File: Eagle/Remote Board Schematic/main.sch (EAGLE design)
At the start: 1 part

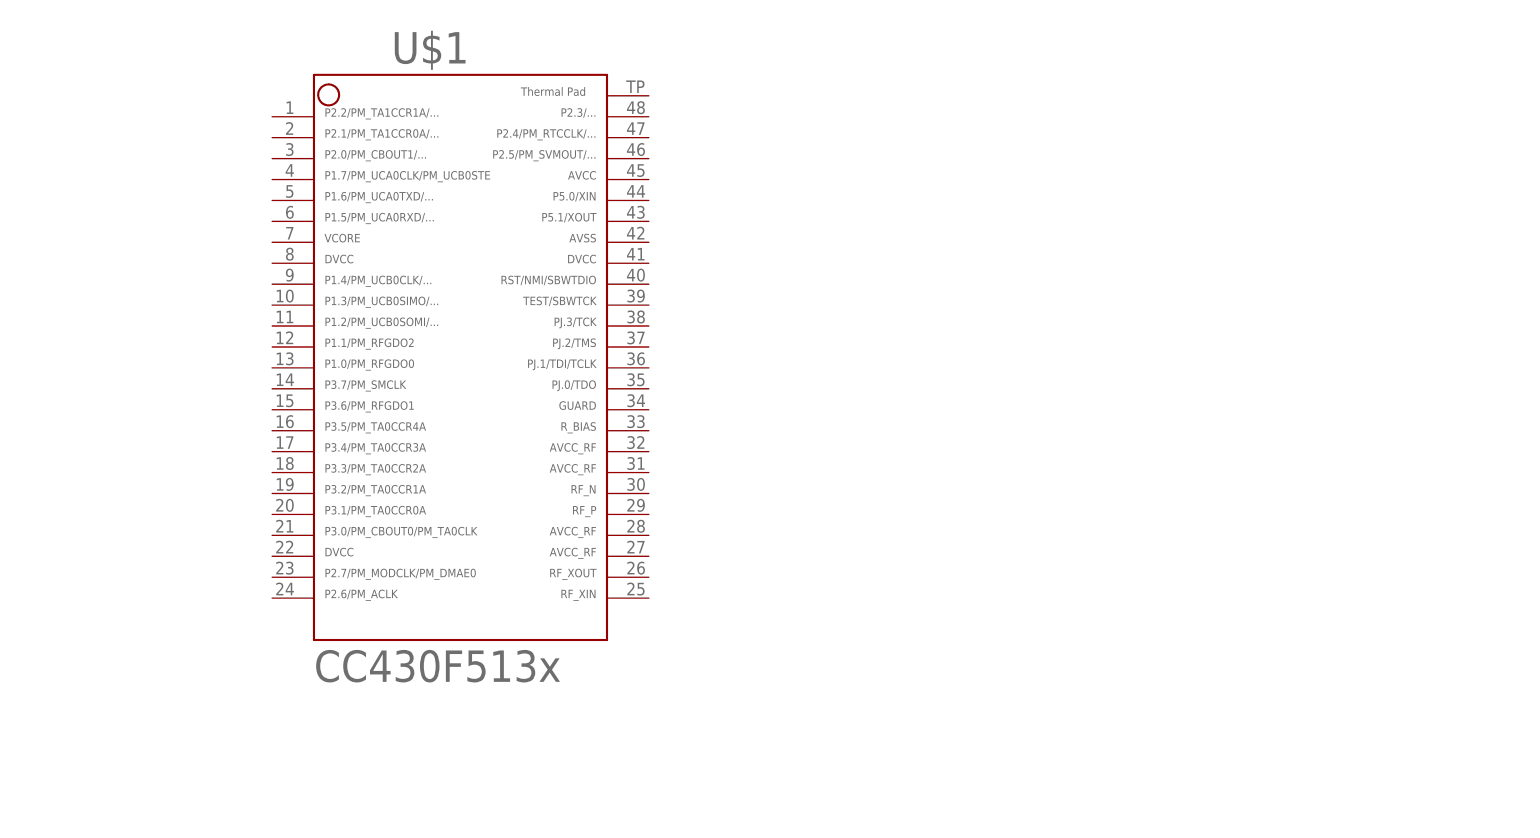
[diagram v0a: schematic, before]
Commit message: Schematic update
Set up skeleton for match network on RF path. Inductor footprint
probably needs to be changed.
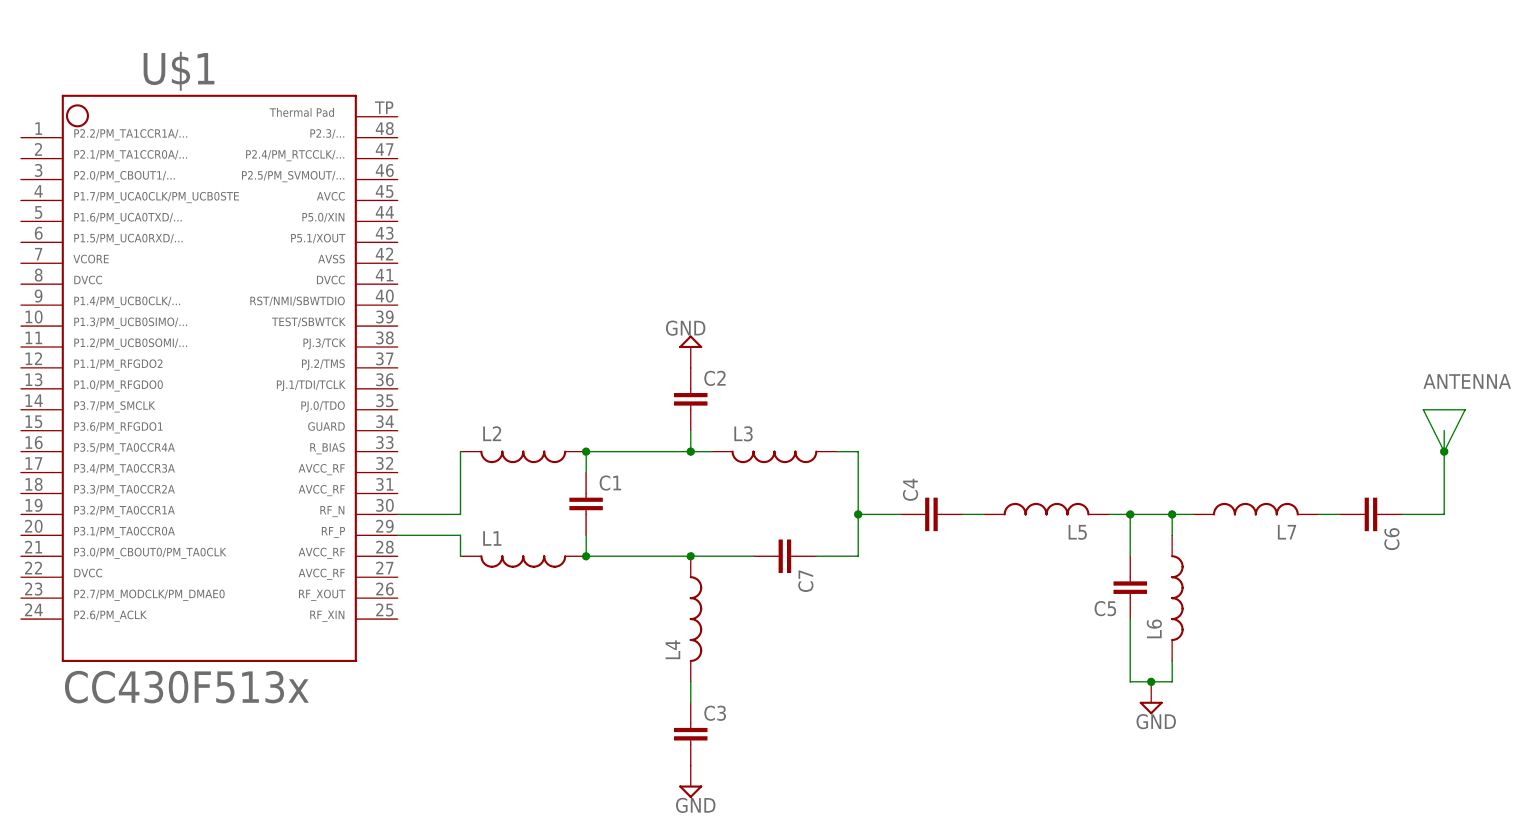
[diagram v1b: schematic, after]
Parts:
- added C1, C2, C3, C4, C5, C6, C7: (no value), rcl:C-EUC0603
- added L1, L2, L3, L4, L5, L6, L7: (no value), resistor:L-USL2012C
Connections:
- new net ANTENNA: C6.1
- new net GND: C2.1, C3.2, C5.1, L6.2
- new net N$1: C1.2, C7.2, L1.1, L4.1
- new net N$10: L1.2, U$1.29
- new net N$2: C1.1, C2.2, L2.1, L3.2
- new net N$3: C4.1, C7.1, L3.1
- new net N$4: C3.1, L4.2
- new net N$5: C4.2, L5.1
- new net N$6: C5.2, L5.2, L6.1, L7.1
- new net N$8: C6.2, L7.2
- new net N$9: L2.2, U$1.30
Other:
- moved on the sheet: U$1

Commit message: Inductors updated with rlc_amber components
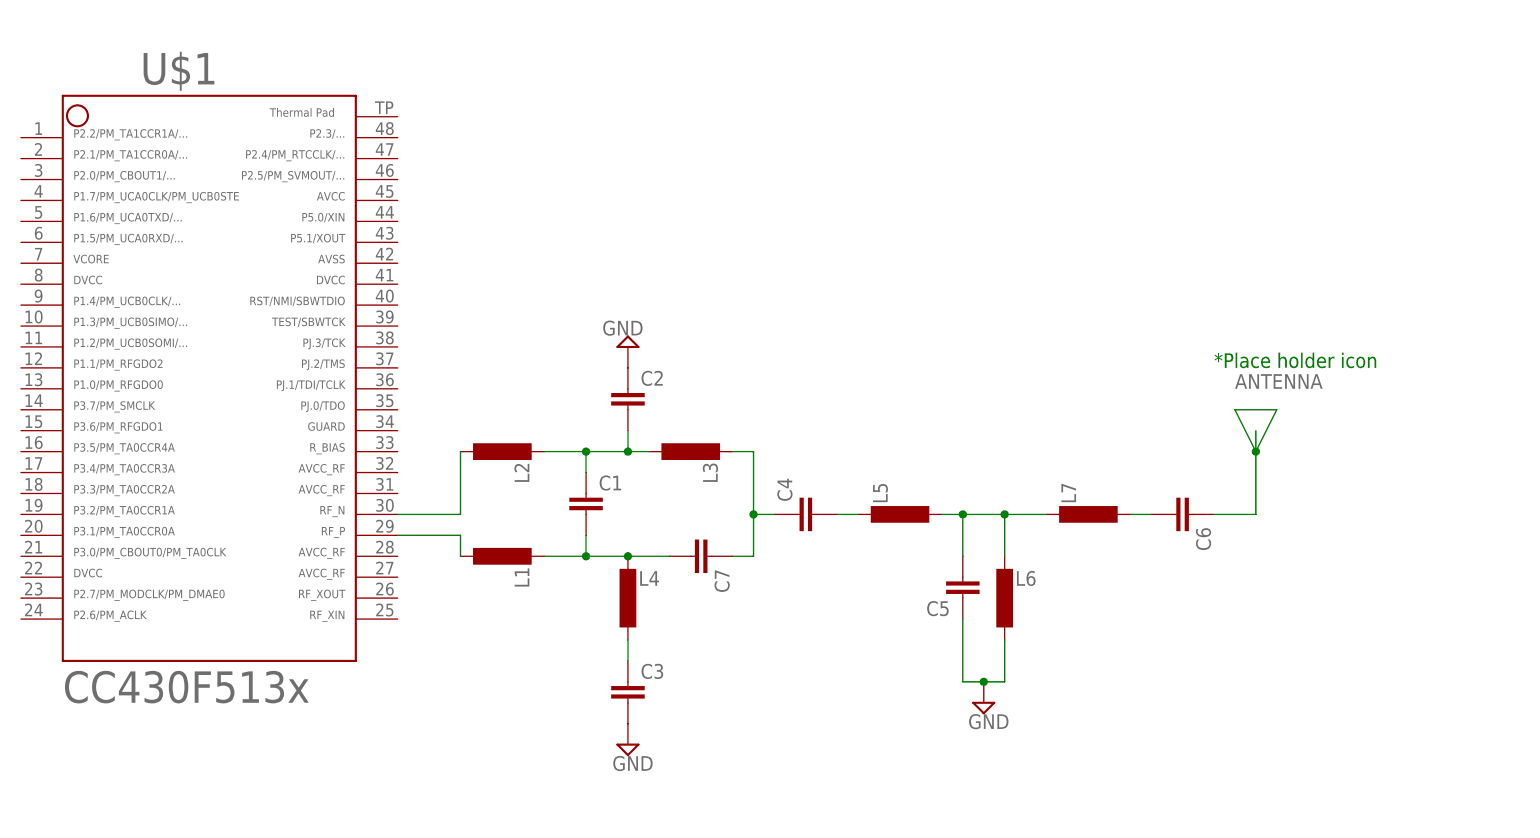
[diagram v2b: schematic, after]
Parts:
- L1, L2, L3, L4, L5, L6, L7: device resistor:L-USL2012C -> rcl-amber:LL0603
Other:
- note added: "*Place holder icon"
- moved on the sheet: C2, C3, C4, C5, C6, C7

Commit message: PCB Antenna Stuff
Baluns and filter network layed out, need to incorperate matching
network (probably pi) and get a footprint kicked out for monopole
antenna. NEED specs on substrate to do this correctly.
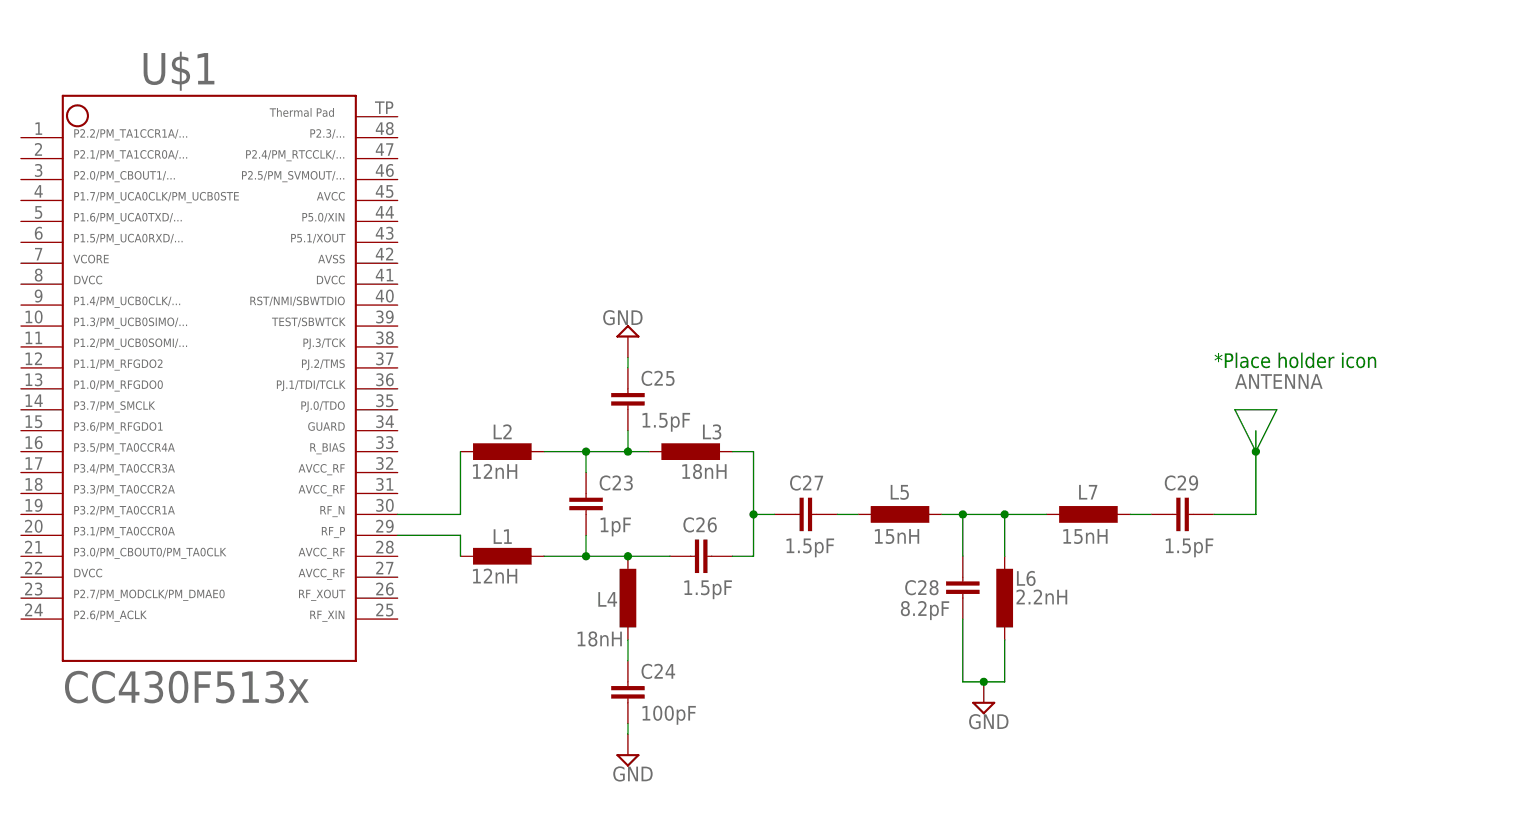
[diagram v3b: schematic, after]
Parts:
- C23: value (none) -> 1pF
- C24: value (none) -> 100pF
- C25, C26, C27, C29: value (none) -> 1.5pF
- C28: value (none) -> 8.2pF
- L1, L2: value (none) -> 12nH
- L3, L4: value (none) -> 18nH
- L5, L7: value (none) -> 15nH
- L6: value (none) -> 2.2nH
- renumbered C1 to C23, C2 to C25, C3 to C24, C4 to C27, C5 to C28, C6 to C29, C7 to C26
